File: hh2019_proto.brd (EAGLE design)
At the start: 51.4 x 60.3 mm, 159 parts, among them IC1 CP210X_USB_UART, IC2 AP2114H, IC4 TP4056, J1 PJ-313D, Q1 MMBT2222A, Q3 MMBT2222A, Q4 MMBT2222A, Q5 SI1304 BDL, Q6 MMBT2222A, U1 MPR121QR2, U2 ESP32-WROVER-I, U3 PCM5102A, X4 JST-PH3

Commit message: Fixed severed F/B annotation
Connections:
- removed net +3V3: C17.1, C20.1, C22.1, C26.1, C27.1, C30.1, C39.1, C43.1, C44.1, C46.1, IC2.4, L1.1, R1.2, R16.2, R22.1, R23.1, R24.1, R28.2, R36.2, T3.2, U1.20, U2.2, X1.10, X1.9
- removed net N$54: U3.P$10
- removed net N$57: C47.2, C48.2, U3.P$20
- removed net N$58: C47.1, C48.1, C53.2, C54.2, U3.P$19
- removed net N$60: C51.2, C52.2, U3.P$1
- removed net N$64: U3.P$11
- removed net N$65: U3.P$12
- removed net N$66: U3.P$16
- net 3V3: now also C17.1, C20.1, C22.1, C26.1, C27.1, C30.1, C39.1, C43.1, C44.1, C46.1, C47.2, C48.2, C51.2, C52.2, IC2.4, L1.1, R1.2, R16.2, R22.1, R23.1, R24.1, R28.2, R36.2, T3.2, U1.20, U2.2, U3.P$1, U3.P$20, X1.10, X1.9
- net GND: now also C47.1, C48.1, C53.2, C54.2, U3.P$10, U3.P$11, U3.P$16, U3.P$19
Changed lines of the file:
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@@
 <contactref element="C51" pad="1"/>
 <contactref element="C52" pad="1"/>
+<contactref element="U3" pad="P$19"/>
+<contactref element="C47" pad="1"/>
+<contactref element="C48" pad="1"/>
+<contactref element="C53" pad="2"/>
+<contactref element="C54" pad="2"/>
+<contactref element="U3" pad="P$10"/>
+<contactref element="U3" pad="P$11"/>
+<contactref element="U3" pad="P$16"/>
 <wire x1="113.173" y1="123.15" x2="114.8" y2="124.85" width="0" layer="19" extent="1-16"/>
 <wire x1="102" y1="124.95" x2="113.173" y2="123.15" width="0" layer="19" extent="1-16"/>
@@
 <wire x1="6.3" y1="7.8" x2="5.7" y2="23.5" width="0" layer="19" extent="1-1"/>
 <wire x1="9.3" y1="5.2" x2="6.3" y2="7.8" width="0" layer="19" extent="1-1"/>
-<wire x1="5.275" y1="-14.3" x2="9.3" y2="5.2" width="0" layer="19" extent="1-1"/>
-<wire x1="1.375" y1="-14.3" x2="5.275" y2="-14.3" width="0" layer="19" extent="1-1"/>
+<wire x1="0.725" y1="-8.7" x2="9.3" y2="5.2" width="0" layer="19" extent="1-1"/>
+<wire x1="1.375" y1="-14.3" x2="0.725" y2="-8.7" width="0" layer="19" extent="1-1"/>
+<wire x1="5.275" y1="-14.3" x2="1.375" y2="-14.3" width="0" layer="19" extent="1-1"/>
 <wire x1="1" y1="-31.5" x2="1.375" y2="-14.3" width="0" layer="19" extent="1-1"/>
 <wire x1="1" y1="-38" x2="1" y2="-31.5" width="0" layer="19" extent="1-1"/>
@@
 <wire x1="-0.35" y1="-45.75" x2="-0.35" y2="-41" width="0" layer="19" extent="1-1"/>
 <wire x1="-0.35" y1="-49.25" x2="-0.35" y2="-45.75" width="0" layer="19" extent="1-1"/>
-<wire x1="1.35" y1="-69.25" x2="-0.35" y2="-49.25" width="0" layer="19" extent="1-1"/>
+<wire x1="-0.35" y1="-54.25" x2="-0.35" y2="-49.25" width="0" layer="19" extent="1-1"/>
+<wire x1="-0.35" y1="-59.25" x2="-0.35" y2="-54.25" width="0" layer="19" extent="1-1"/>
+<wire x1="1.35" y1="-69.25" x2="-0.35" y2="-59.25" width="0" layer="19" extent="1-1"/>
 <wire x1="-0.35" y1="-74.25" x2="1.35" y2="-69.25" width="0" layer="19" extent="1-1"/>
 <wire x1="-0.35" y1="-79.25" x2="-0.35" y2="-74.25" width="0" layer="19" extent="1-1"/>
+<wire x1="1.35" y1="-84.25" x2="-0.35" y2="-79.25" width="0" layer="19" extent="1-1"/>
+<wire x1="1.35" y1="-89.25" x2="1.35" y2="-84.25" width="0" layer="19" extent="1-1"/>
 <wire x1="90.6" y1="30" x2="67.9" y2="44" width="0" layer="19" extent="1-1"/>
 <wire x1="88.6" y1="6.1" x2="90.6" y2="30" width="0" layer="19" extent="1-1"/>
@@
 <wire x1="43.8" y1="72.25" x2="45.3" y2="73.4" width="0" layer="19" extent="1-1"/>
 </signal>
-<signal name="+3V3">
+<signal name="3V3">
 <contactref element="X1" pad="10"/>
 <contactref element="X1" pad="9"/>
@@
 <contactref element="C46" pad="1"/>
 <contactref element="U2" pad="2"/>
+<contactref element="U3" pad="P$8"/>
+<contactref element="C37" pad="2"/>
+<contactref element="C40" pad="2"/>
+<contactref element="U3" pad="P$20"/>
+<contactref element="C47" pad="2"/>
+<contactref element="C48" pad="2"/>
+<contactref element="U3" pad="P$1"/>
+<contactref element="C51" pad="2"/>
+<contactref element="C52" pad="2"/>
 <wire x1="131.4" y1="98.45" x2="130.9" y2="98.45" width="0" layer="19" extent="1-1"/>
 <wire x1="129.94" y1="94.97" x2="130.9" y2="98.45" width="0" layer="19" extent="1-1"/>
@@
 <wire x1="128.849" y1="13.259" x2="128.9045" y2="14.967" width="0" layer="19" extent="1-1"/>
 <wire x1="128.770971875" y1="11.029525" x2="128.849" y2="13.259" width="0" layer="19" extent="1-1"/>
+<wire x1="0.073" y1="-8.7" x2="23.8" y2="48.05" width="0" layer="19" extent="1-1"/>
+<wire x1="0.075" y1="-14.3" x2="0.073" y2="-8.7" width="0" layer="19" extent="1-1"/>
+<wire x1="4.625" y1="-14.3" x2="0.075" y2="-14.3" width="0" layer="19" extent="1-1"/>
+<wire x1="1.35" y1="-45.75" x2="0.075" y2="-14.3" width="0" layer="19" extent="1-1"/>
+<wire x1="1.35" y1="-49.25" x2="1.35" y2="-45.75" width="0" layer="19" extent="1-1"/>
+<wire x1="1.35" y1="-54.25" x2="1.35" y2="-49.25" width="0" layer="19" extent="1-1"/>
+<wire x1="1.35" y1="-59.25" x2="1.35" y2="-54.25" width="0" layer="19" extent="1-1"/>
+<wire x1="1.35" y1="-74.25" x2="1.35" y2="-59.25" width="0" layer="19" extent="1-1"/>
+<wire x1="1.35" y1="-79.25" x2="1.35" y2="-74.25" width="0" layer="19" extent="1-1"/>
 </signal>
 <signal name="GDR">
@@
 <contactref element="U3" pad="P$6"/>
 </signal>
-<signal name="3V3">
-<contactref element="U3" pad="P$8"/>
-<contactref element="C37" pad="2"/>
-<contactref element="C40" pad="2"/>
-<wire x1="1.35" y1="-45.75" x2="1.35" y2="-49.25" width="0" layer="19" extent="1-1"/>
-<wire x1="4.625" y1="-14.3" x2="1.35" y2="-45.75" width="0" layer="19" extent="1-1"/>
-</signal>
-<signal name="N$54">
-<contactref element="U3" pad="P$10"/>
-</signal>
 <signal name="N$55">
 <contactref element="U3" pad="P$4"/>
@@
 <contactref element="C49" pad="1"/>
 <wire x1="0.725" y1="-14.3" x2="-0.35" y2="-64.25" width="0" layer="19" extent="1-1"/>
-</signal>
-<signal name="N$57">
-<contactref element="U3" pad="P$20"/>
-<contactref element="C47" pad="2"/>
-<contactref element="C48" pad="2"/>
-<wire x1="1.35" y1="-54.25" x2="1.35" y2="-59.25" width="0" layer="19" extent="1-1"/>
-<wire x1="0.073" y1="-8.7" x2="1.35" y2="-54.25" width="0" layer="19" extent="1-1"/>
-</signal>
-<signal name="N$58">
-<contactref element="U3" pad="P$19"/>
-<contactref element="C47" pad="1"/>
-<contactref element="C48" pad="1"/>
-<contactref element="C53" pad="2"/>
-<contactref element="C54" pad="2"/>
-<wire x1="1.35" y1="-84.25" x2="1.35" y2="-89.25" width="0" layer="19" extent="1-1"/>
-<wire x1="-0.35" y1="-59.25" x2="1.35" y2="-84.25" width="0" layer="19" extent="1-1"/>
-<wire x1="-0.35" y1="-54.25" x2="-0.35" y2="-59.25" width="0" layer="19" extent="1-1"/>
-<wire x1="0.725" y1="-8.7" x2="-0.35" y2="-54.25" width="0" layer="19" extent="1-1"/>
 </signal>
 <signal name="N$59">
@@
 <wire x1="1.375" y1="-8.7" x2="-0.35" y2="-84.25" width="0" layer="19" extent="1-1"/>
 </signal>
-<signal name="N$60">
-<contactref element="U3" pad="P$1"/>
-<contactref element="C51" pad="2"/>
-<contactref element="C52" pad="2"/>
-<wire x1="1.35" y1="-74.25" x2="1.35" y2="-79.25" width="0" layer="19" extent="1-1"/>
-<wire x1="0.075" y1="-14.3" x2="1.35" y2="-74.25" width="0" layer="19" extent="1-1"/>
-</signal>
 <signal name="N$62">
 <contactref element="U3" pad="P$5"/>
@@
 <wire x1="2.675" y1="-14.3" x2="-0.35" y2="-69.25" width="0" layer="19" extent="1-1"/>
 </signal>
-<signal name="N$64">
-<contactref element="U3" pad="P$11"/>
-</signal>
-<signal name="N$65">
-<contactref element="U3" pad="P$12"/>
-</signal>
-<signal name="N$66">
-<contactref element="U3" pad="P$16"/>
-</signal>
 </signals>

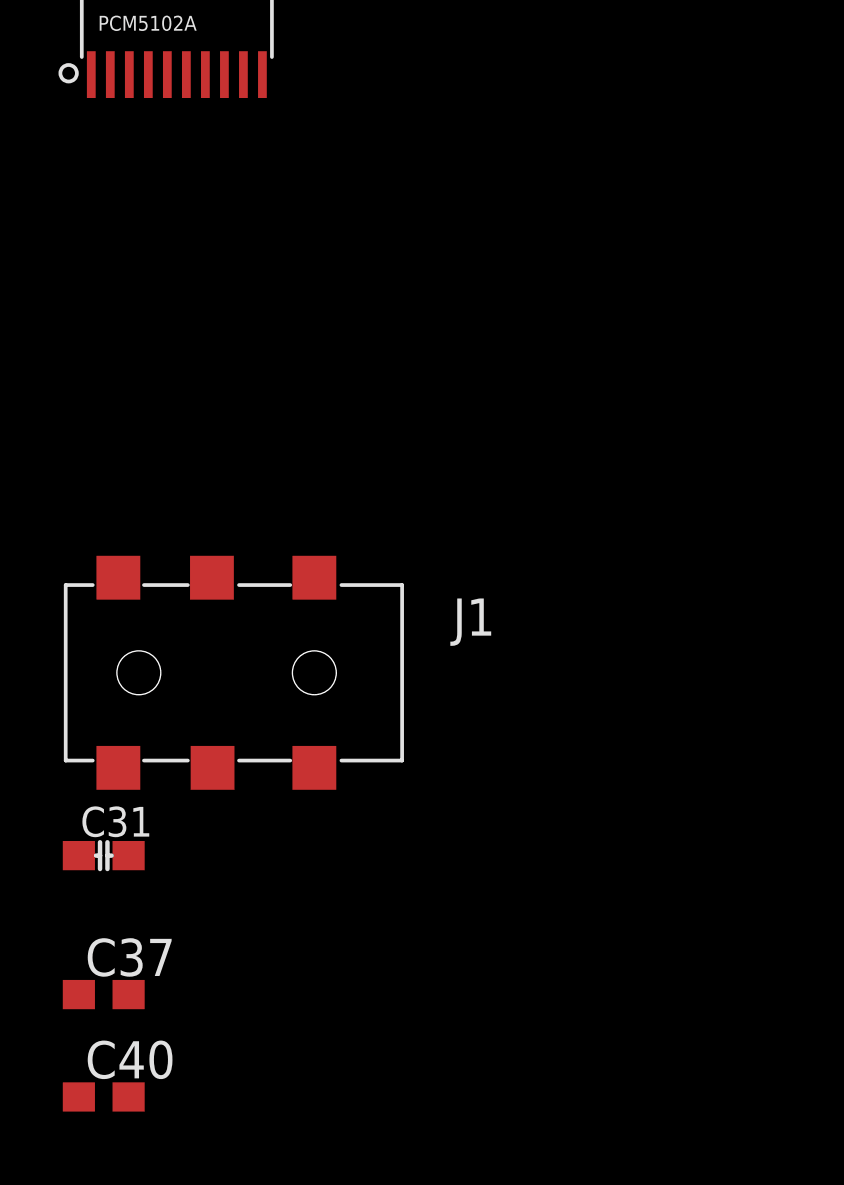
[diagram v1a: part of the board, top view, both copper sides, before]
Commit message: Fixed net names on DAC
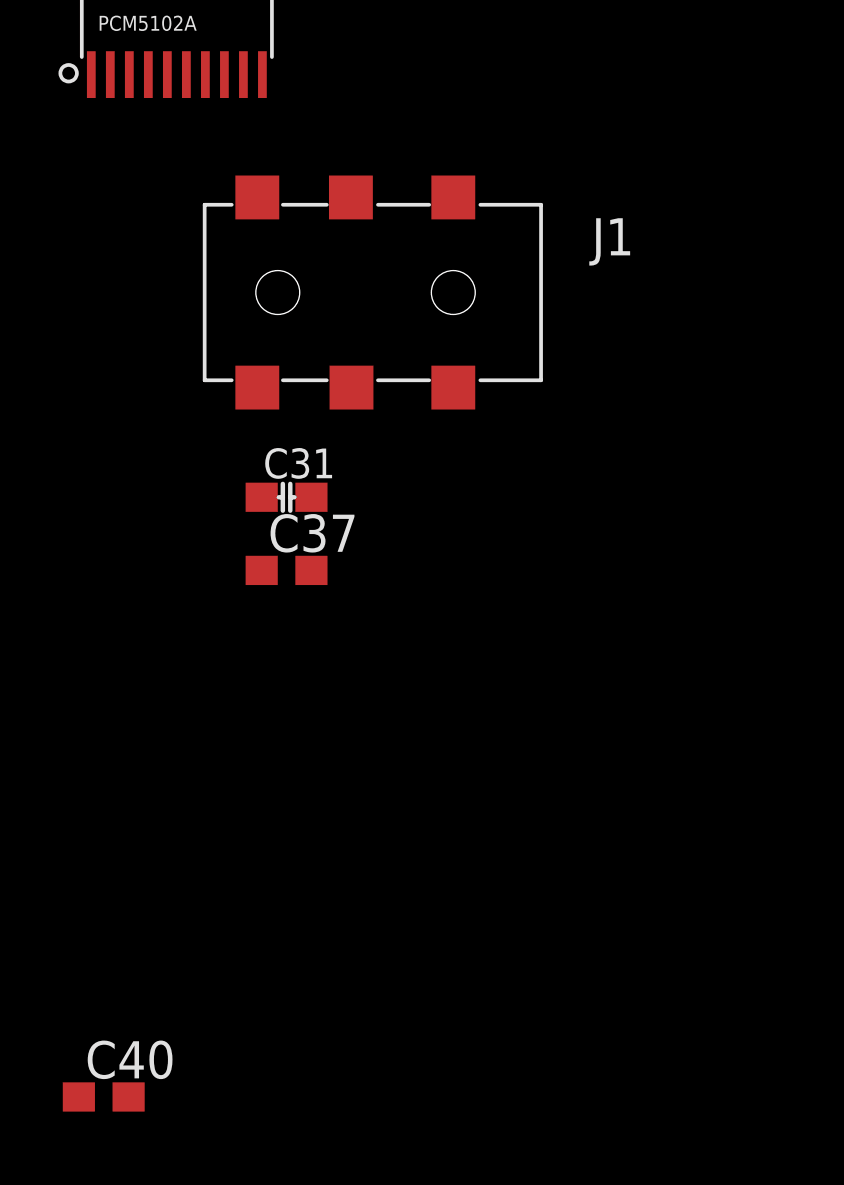
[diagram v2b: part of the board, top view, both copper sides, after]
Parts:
- moved C37 15.8 mm to (6.75, -31.2)
- moved J1 13.8 mm to (5.75, -21.8)
- moved C31 13.8 mm to (6.75, -28.8)
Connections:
- net I2S_SCK: now also U2.16
- net I2S_SD: now also U2.24
- net I2S_WS: now also U2.23
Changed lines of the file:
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@@
 <attribute name="VALUE" x="0.3" y="-12.8" size="0.508" layer="25" font="vector"/>
 </element>
-<element name="J1" library="audioconn" package="PJ-313D" value="PJ-313D" x="1" y="-34.75" smashed="yes">
-<attribute name="NAME" x="12.43" y="-33.48" size="1.27" layer="25"/>
-<attribute name="VALUE" x="12.43" y="-36.02" size="1.27" layer="27"/>
-</element>
-<element name="C31" library="hh2019_proto" package="C0603-DASHES" value="100n" x="0.5" y="-41" smashed="yes">
-<attribute name="MF" value="" x="0.5" y="-41" size="1.778" layer="27" display="off"/>
-<attribute name="MPN" value="" x="0.5" y="-41" size="1.778" layer="27" display="off"/>
-<attribute name="NAME" x="-0.3" y="-40.35" size="1.016" layer="25"/>
-<attribute name="OC_FARNELL" value="unknown" x="0.5" y="-41" size="1.778" layer="27" display="off"/>
-<attribute name="PARTNO" value="GRM188R71H104KA93D" x="0.5" y="-41" size="1.778" layer="27" display="off"/>
-<attribute name="VALUE" x="-0.3" y="-42.65" size="1.016" layer="27"/>
-</element>
-<element name="C37" library="rcl" library_urn="urn:adsk.eagle:library:334" package="C0603" package3d_urn="urn:adsk.eagle:package:23616/2" value="100n" x="0.5" y="-45.75" smashed="yes">
-<attribute name="NAME" x="-0.135" y="-45.115" size="1.27" layer="25"/>
-<attribute name="SPICEPREFIX" value="C" x="0.5" y="-45.75" size="1.778" layer="27" display="off"/>
-<attribute name="VALUE" x="-0.135" y="-47.655" size="1.27" layer="27"/>
+<element name="J1" library="audioconn" package="PJ-313D" value="PJ-313D" x="5.75" y="-21.75" smashed="yes">
+<attribute name="NAME" x="17.18" y="-20.48" size="1.27" layer="25"/>
+<attribute name="VALUE" x="17.18" y="-23.02" size="1.27" layer="27"/>
+</element>
+<element name="C31" library="hh2019_proto" package="C0603-DASHES" value="100n" x="6.75" y="-28.75" smashed="yes">
+<attribute name="MF" value="" x="6.75" y="-28.75" size="1.778" layer="27" display="off"/>
+<attribute name="MPN" value="" x="6.75" y="-28.75" size="1.778" layer="27" display="off"/>
+<attribute name="NAME" x="5.95" y="-28.1" size="1.016" layer="25"/>
+<attribute name="OC_FARNELL" value="unknown" x="6.75" y="-28.75" size="1.778" layer="27" display="off"/>
+<attribute name="PARTNO" value="GRM188R71H104KA93D" x="6.75" y="-28.75" size="1.778" layer="27" display="off"/>
+<attribute name="VALUE" x="5.95" y="-30.4" size="1.016" layer="27"/>
+</element>
+<element name="C37" library="rcl" library_urn="urn:adsk.eagle:library:334" package="C0603" package3d_urn="urn:adsk.eagle:package:23616/2" value="100n" x="6.75" y="-31.25" smashed="yes">
+<attribute name="NAME" x="6.115" y="-30.615" size="1.27" layer="25"/>
+<attribute name="SPICEPREFIX" value="C" x="6.75" y="-31.25" size="1.778" layer="27" display="off"/>
+<attribute name="VALUE" x="6.115" y="-33.155" size="1.27" layer="27"/>
 </element>
 <element name="C40" library="rcl" library_urn="urn:adsk.eagle:library:334" package="C0603" package3d_urn="urn:adsk.eagle:package:23616/2" value="1u" x="0.5" y="-49.25" smashed="yes">
@@
 <wire x1="1.375" y1="-14.3" x2="0.725" y2="-8.7" width="0" layer="19" extent="1-1"/>
 <wire x1="5.275" y1="-14.3" x2="1.375" y2="-14.3" width="0" layer="19" extent="1-1"/>
-<wire x1="1" y1="-31.5" x2="1.375" y2="-14.3" width="0" layer="19" extent="1-1"/>
-<wire x1="1" y1="-38" x2="1" y2="-31.5" width="0" layer="19" extent="1-1"/>
-<wire x1="-0.35" y1="-41" x2="1" y2="-38" width="0" layer="19" extent="1-1"/>
-<wire x1="-0.35" y1="-45.75" x2="-0.35" y2="-41" width="0" layer="19" extent="1-1"/>
-<wire x1="-0.35" y1="-49.25" x2="-0.35" y2="-45.75" width="0" layer="19" extent="1-1"/>
+<wire x1="5.75" y1="-18.5" x2="1.375" y2="-14.3" width="0" layer="19" extent="1-1"/>
+<wire x1="5.75" y1="-25" x2="5.75" y2="-18.5" width="0" layer="19" extent="1-1"/>
+<wire x1="5.9" y1="-28.75" x2="5.75" y2="-25" width="0" layer="19" extent="1-1"/>
+<wire x1="5.9" y1="-31.25" x2="5.9" y2="-28.75" width="0" layer="19" extent="1-1"/>
+<wire x1="-0.35" y1="-49.25" x2="5.9" y2="-31.25" width="0" layer="19" extent="1-1"/>
 <wire x1="-0.35" y1="-54.25" x2="-0.35" y2="-49.25" width="0" layer="19" extent="1-1"/>
 <wire x1="-0.35" y1="-59.25" x2="-0.35" y2="-54.25" width="0" layer="19" extent="1-1"/>
@@
 <wire x1="0.075" y1="-14.3" x2="0.073" y2="-8.7" width="0" layer="19" extent="1-1"/>
 <wire x1="4.625" y1="-14.3" x2="0.075" y2="-14.3" width="0" layer="19" extent="1-1"/>
-<wire x1="1.35" y1="-45.75" x2="0.075" y2="-14.3" width="0" layer="19" extent="1-1"/>
-<wire x1="1.35" y1="-49.25" x2="1.35" y2="-45.75" width="0" layer="19" extent="1-1"/>
+<wire x1="7.6" y1="-31.25" x2="0.075" y2="-14.3" width="0" layer="19" extent="1-1"/>
+<wire x1="1.35" y1="-49.25" x2="7.6" y2="-31.25" width="0" layer="19" extent="1-1"/>
 <wire x1="1.35" y1="-54.25" x2="1.35" y2="-49.25" width="0" layer="19" extent="1-1"/>
 <wire x1="1.35" y1="-59.25" x2="1.35" y2="-54.25" width="0" layer="19" extent="1-1"/>
@@
 <contactref element="C31" pad="2"/>
 <wire x1="116.55" y1="65.1" x2="116.32" y2="68.44" width="0" layer="19" extent="1-1"/>
-<wire x1="1.35" y1="-41" x2="116.55" y2="65.1" width="0" layer="19" extent="1-1"/>
+<wire x1="7.6" y1="-28.75" x2="116.55" y2="65.1" width="0" layer="19" extent="1-1"/>
 </signal>
 <signal name="N$2">
@@
 <signal name="I2S_WS">
 <contactref element="U3" pad="P$15"/>
+<contactref element="U2" pad="23"/>
+<wire x1="3.325" y1="-8.7" x2="130.29" y2="86.06" width="0" layer="19" extent="1-1"/>
 </signal>
 <signal name="I2S_SCK">
 <contactref element="U3" pad="P$13"/>
+<contactref element="U2" pad="16"/>
+<wire x1="4.625" y1="-8.7" x2="130.29" y2="68.44" width="0" layer="19" extent="1-1"/>
 </signal>
 <signal name="I2S_SD">
 <contactref element="U3" pad="P$14"/>
+<contactref element="U2" pad="24"/>
+<wire x1="3.975" y1="-8.7" x2="129.02" y2="86.06" width="0" layer="19" extent="1-1"/>
 </signal>
 <signal name="AUDIO_L">
 <contactref element="J1" pad="4_1"/>
 <contactref element="J1" pad="4_2"/>
-<wire x1="7.7" y1="-31.5" x2="7.7" y2="-38" width="0" layer="19" extent="1-1"/>
+<wire x1="12.45" y1="-18.5" x2="12.45" y2="-25" width="0" layer="19" extent="1-1"/>
 </signal>
 <signal name="AUDIO_R">
 <contactref element="J1" pad="3_1"/>
 <contactref element="J1" pad="3_2"/>
-<wire x1="4.2" y1="-31.5" x2="4.22" y2="-38" width="0" layer="19" extent="1-1"/>
+<wire x1="8.95" y1="-18.5" x2="8.97" y2="-25" width="0" layer="19" extent="1-1"/>
 </signal>
 <signal name="N$16">

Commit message: Fixed ESP32 net labels, removed SD card components, working on layout
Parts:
- removed C12, C7: 100n, hh2019_proto:C0603-DASHES
- removed C41: 4u7/16V, rcl:C0805
- removed D2: NSVR0320MW2T1G, SparkFun-DiscreteSemi:SOD-323
- removed Q6: MMBT2222A, SparkFun-DiscreteSemi:SOT23-3
- removed R27, R28, R5: 10k, 00ralf:R0603-DASHES
- removed T3: (no value), SparkFun-DiscreteSemi:SOT23-3
- moved C40 346.8 mm to (323.9, 76.2)
- moved C54 332.1 mm to (301.0, 52.1), turned to 90 degrees
- moved C53 327.7 mm to (298.4, 52.1), turned to 90 degrees
- moved C52 327.6 mm to (302.3, 48.3), turned to 270 degrees
- moved C37 326.4 mm to (315.0, 76.2)
- moved C51 323.3 mm to (299.7, 48.3), turned to 270 degrees
- moved C48 321.5 mm to (303.5, 48.3), turned to 270 degrees
- moved C50 315.9 mm to (297.2, 39.4), turned to 180 degrees
- moved C49 315.1 mm to (297.2, 41.9)
- moved C47 310.1 mm to (285.8, 67.3)
- moved C39 306.3 mm to (323.9, 110.5), turned to 270 degrees
- moved U3 305.2 mm to (303.5, 41.9)
- moved J1 302.1 mm to (303.5, 29.2), turned to 270 degrees
- moved C27 295.8 mm to (262.9, 210.8), turned to 0 degrees
- moved TOUCH_B 287.7 mm to (-135.9, 40.6)
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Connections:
- net N$55 renamed CAPM
- net N$56 renamed CAPP
- net N$59 renamed LDO0
- net N$62 renamed VNEG
- removed net 3V3_SWITCHED: C12.1, C41.1, C7.1, R5.2, T3.3
- removed net N$15: Q6.1, R27.2
- removed net N$16: U3.P$7
- removed net N$17: Q6.3, R28.1, T3.1
- removed net N$18: U3.P$6
- removed net N$49: C34.1, F2.1, IC4.5, X4.3
- removed net SD_DATA0: D2.A, R5.1
- new net DEMP: U3.P$10
- net 3V3: no longer R28.2, T3.2
- net AUDIO_L: now also U3.P$6
- net AUDIO_R: now also U3.P$7
- net ESP32_FLASH: no longer D2.C
- net GND: no longer C12.2, C41.2, C7.2, Q6.2, U3.P$10
- net VBAT: now also C34.1, F2.1, IC4.5, X4.3
- net WS2812_POWER_EN: no longer R27.1
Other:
- board size 51.4 x 60.3 mm -> 263.1 x 150 mm
